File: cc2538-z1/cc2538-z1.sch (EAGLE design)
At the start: 101 parts, among them U1 CC2538, U10 DMG6602SVT, U2 CC1120_RHM_32, U3 TPD2E001IDRLRQ1, U4 CP2103, U5 BSS138PS, U6 BSS138PS, U7 BSS138PS, U8 M25P16VMN6P, U9 DMG6602SVT, X1 FA-128, X2 32MHz, X3 32.768K

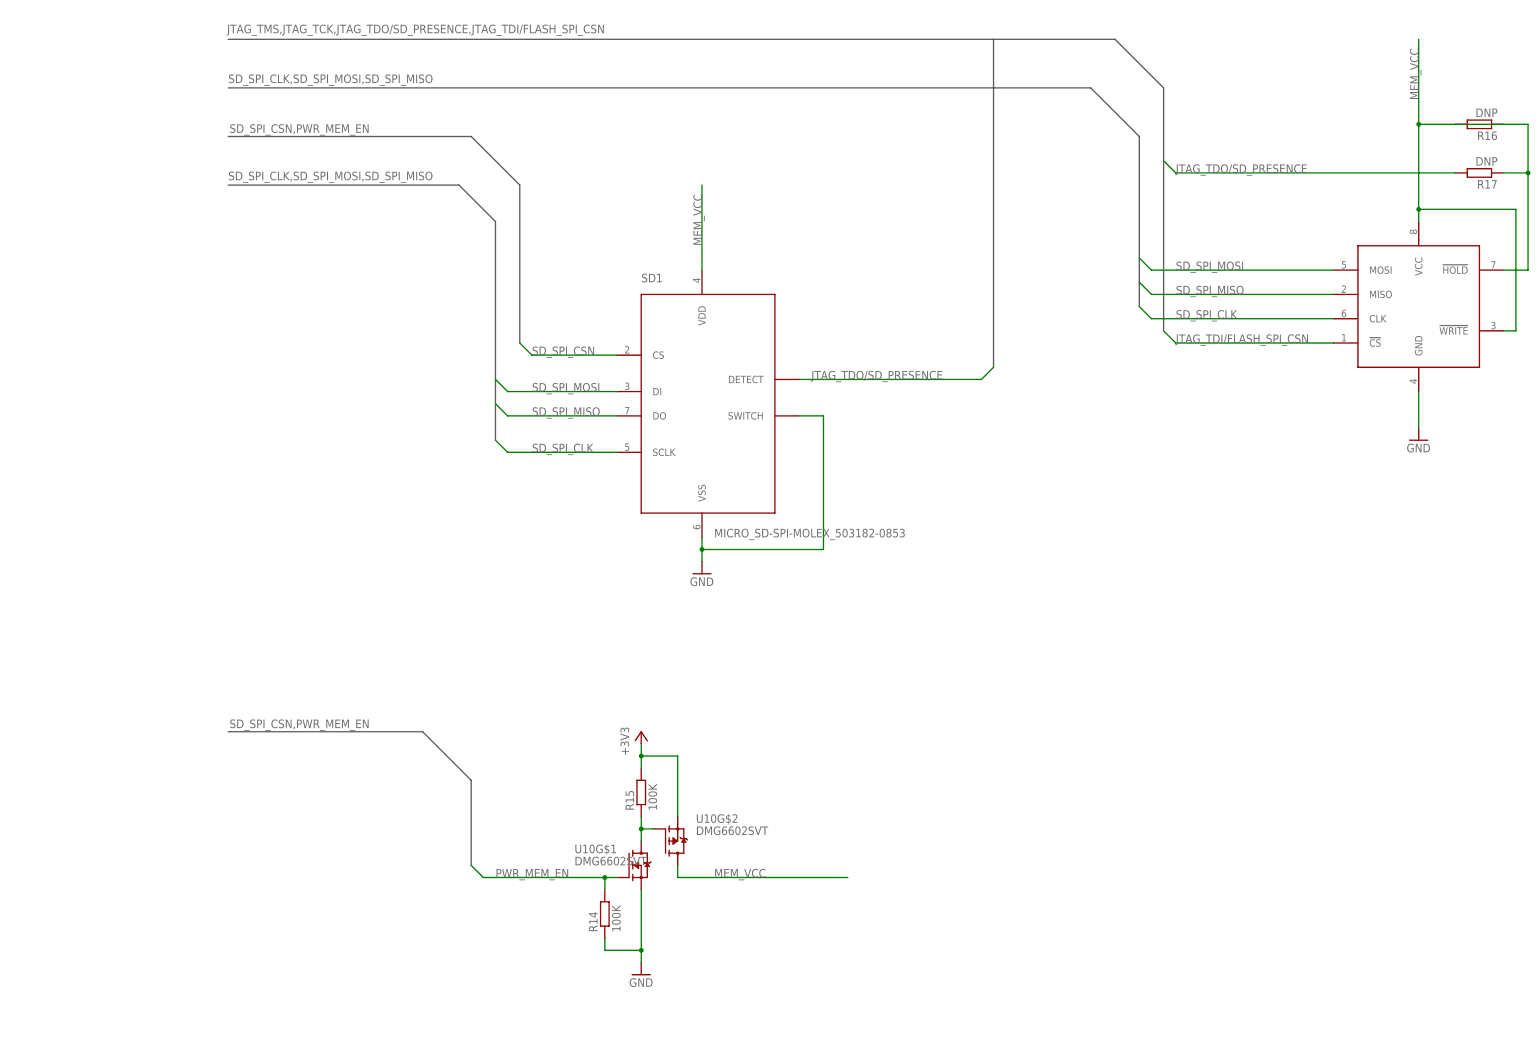
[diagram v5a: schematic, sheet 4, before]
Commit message: Added level translator for SPI power down, resized some DNP resistors, some other minor changes.
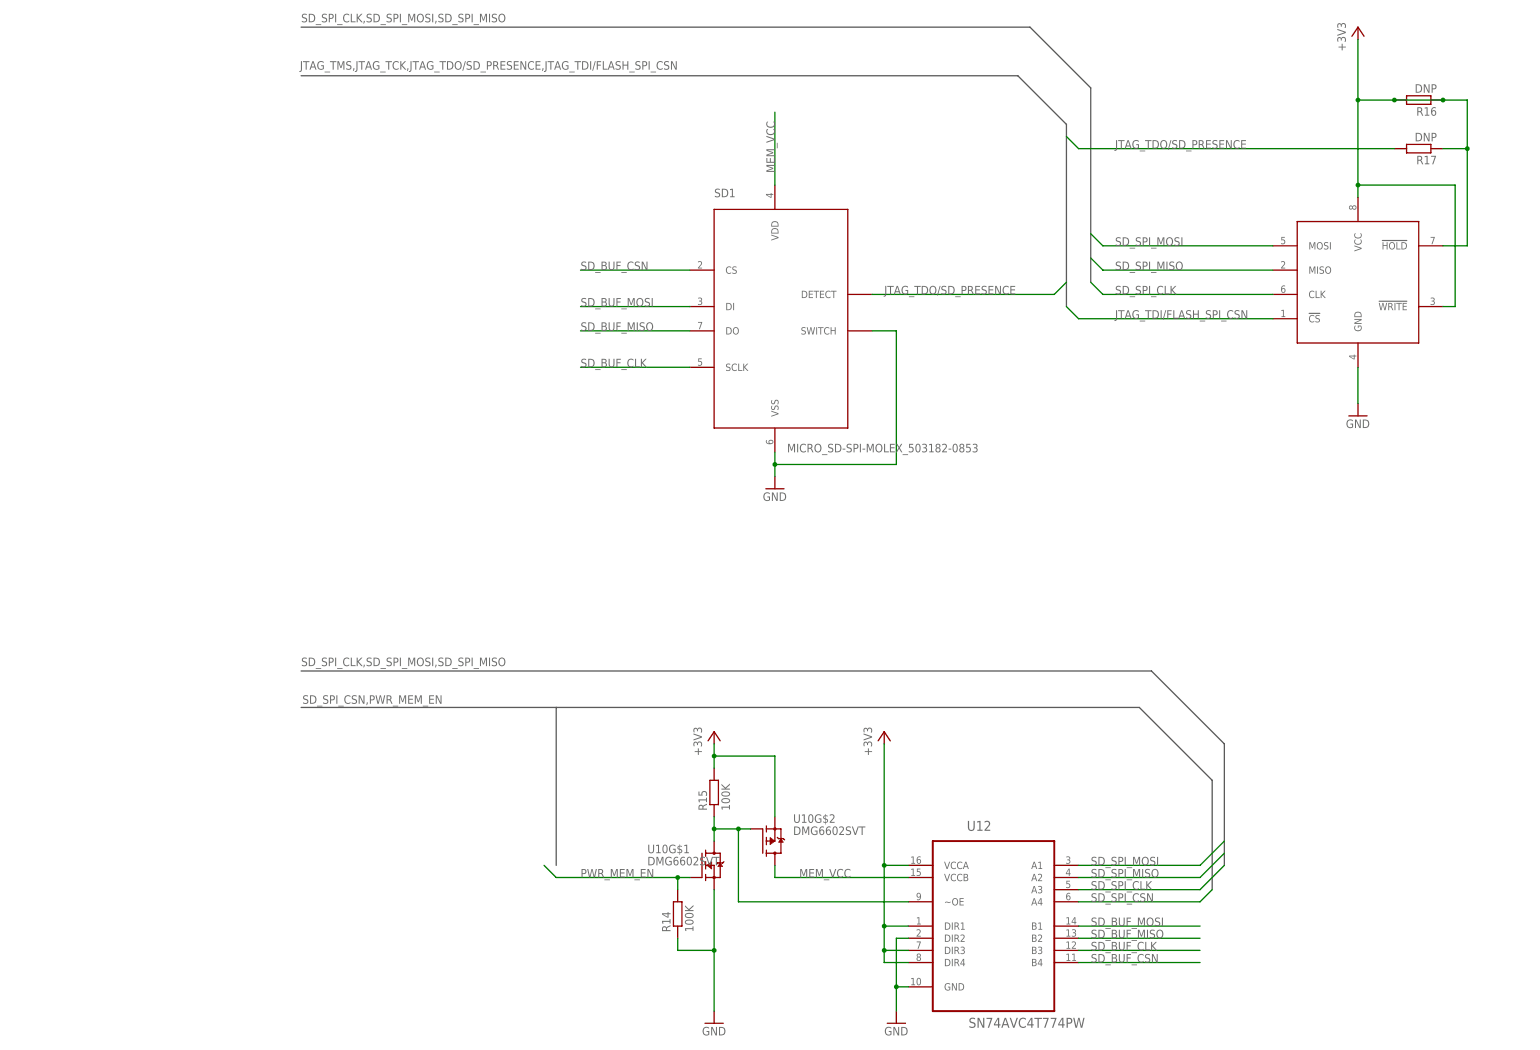
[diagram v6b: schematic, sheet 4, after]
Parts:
- added U12: SN74AVC4T774PW, CC11x:SN74AVC4T774PW
- R1, R2, R3, R4, R5, R6, R7: value (none) -> DNP; device rcl:R-EU_R0603 -> rcl:R-EU_R0402
- R16, R17: device rcl:R-EU_R0603 -> rcl:R-EU_R0402
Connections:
- removed net N$43: R15.1, U10G$1.D@1, U10G$2.G
- removed net N$65: U1.DVDD_USB
- removed net N$66: U1.USB_N
- removed net N$67: U1.USB_P
- removed net N$68: U1.DGND_USB
- new net N$42: R15.1, U10G$1.D@1, U10G$2.G, U12.~OE
- new net SD_BUF_CLK: SD1.SCLK, U12.B3
- new net SD_BUF_CSN: SD1.CS, U12.B4
- new net SD_BUF_MISO: SD1.DO, U12.B2
- new net SD_BUF_MOSI: SD1.DI, U12.B1
- net +3V3: now also R16.1, R16.2, R17.1, U12.DIR1, U12.DIR3, U12.DIR4, U12.VCCA, U8.!HOLD, U8.!WRITE, U8.VCC
- net GND: now also U1.DGND_USB, U1.DVDD_USB, U1.USB_N, U1.USB_P, U12.DIR2, U12.GND
- net MEM_VCC: now also U12.VCCB; no longer R16.1, R16.2, R17.1, U8.!HOLD, U8.!WRITE, U8.VCC
- net SD_SPI_CLK: now also U12.A3; no longer SD1.SCLK
- net SD_SPI_CSN: now also U12.A4; no longer SD1.CS
- net SD_SPI_MISO: now also U12.A2; no longer SD1.DO
- net SD_SPI_MOSI: now also U12.A1; no longer SD1.DI
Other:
- moved on the sheet: C10, R1, R14, R15, R16, R17, R2, R3, R4, R5, SD1, U10G$1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

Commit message: Finalised board design?
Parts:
- added C20, C22: 1uF, CC11x:C_EUC0603S
- added C23: 100nF, CC11x:C_EUC0603S
- added U11: SN74AVC4T774PW, CC11x:SN74AVC4T774PW
- R10: value (none) -> 100k
- U12: value SN74AVC4T774PW -> TMP102AIDRLT; device CC11x:SN74AVC4T774PW -> CC11x:TMP102AIDRLT
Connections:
- removed net N$20: J1.4, R10.2
- removed net N$40: H1.ALERT
- removed net N$64: H1.TEMP_PMR
- new net TEMP_ALERT: H1.ALERT, U12.ALERT
- net +3V3: now also C22.2, C23.2, U11.DIR1, U11.DIR3, U11.DIR4, U11.VCCA; no longer U12.DIR1, U12.DIR3, U12.DIR4, U12.VCCA
- net GND: now also C20.2, C22.1, C23.1, U11.DIR2, U11.GND, U12.ADD0, U6.D1, U6.G1, U6.S1; no longer U12.DIR2
- net GNDA: no longer R10.1
- net I2C_SCL: now also U12.SCL
- net I2C_SDA: now also U12.SDA
- net JTAG_TDO/SD_PRESENCE: now also C20.1, R10.1
- net MEM_VCC: now also R10.2, U11.VCCB; no longer U12.VCCB
- net N$42: now also U11.~OE; no longer U12.~OE
- net PWR_SENSE_EN: now also H1.TEMP_PMR, U12.V+
- net SD_BUF_CLK: now also U11.B3; no longer U12.B3
- net SD_BUF_CSN: now also U11.B4; no longer U12.B4
- net SD_BUF_MISO: now also U11.B2; no longer U12.B2
- net SD_BUF_MOSI: now also U11.B1; no longer U12.B1
- net SD_SPI_CLK: now also U11.A3; no longer U12.A3
- net SD_SPI_CSN: now also U11.A4; no longer U12.A4
- net SD_SPI_MISO: now also U11.A2; no longer U12.A2
- net SD_SPI_MOSI: now also U11.A1; no longer U12.A1
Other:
- moved on the sheet: C16, C17, C18, C19, D1, L2, L3, L5
